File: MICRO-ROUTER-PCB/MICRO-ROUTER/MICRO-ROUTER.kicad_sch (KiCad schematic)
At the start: 41 parts, among them J1 SMA, J2 USB_A, J3 USB_C_Receptacle_USB2.0_16P, J4 Battery Connector, J5 SPI Header, J6 GPIO Header, Q1 FS8205A, SW2 8Devices Reset, SW3 UART Reset, U1 TP4056, U3 CP2102N-Axx-xQFN20, U4 DW01A

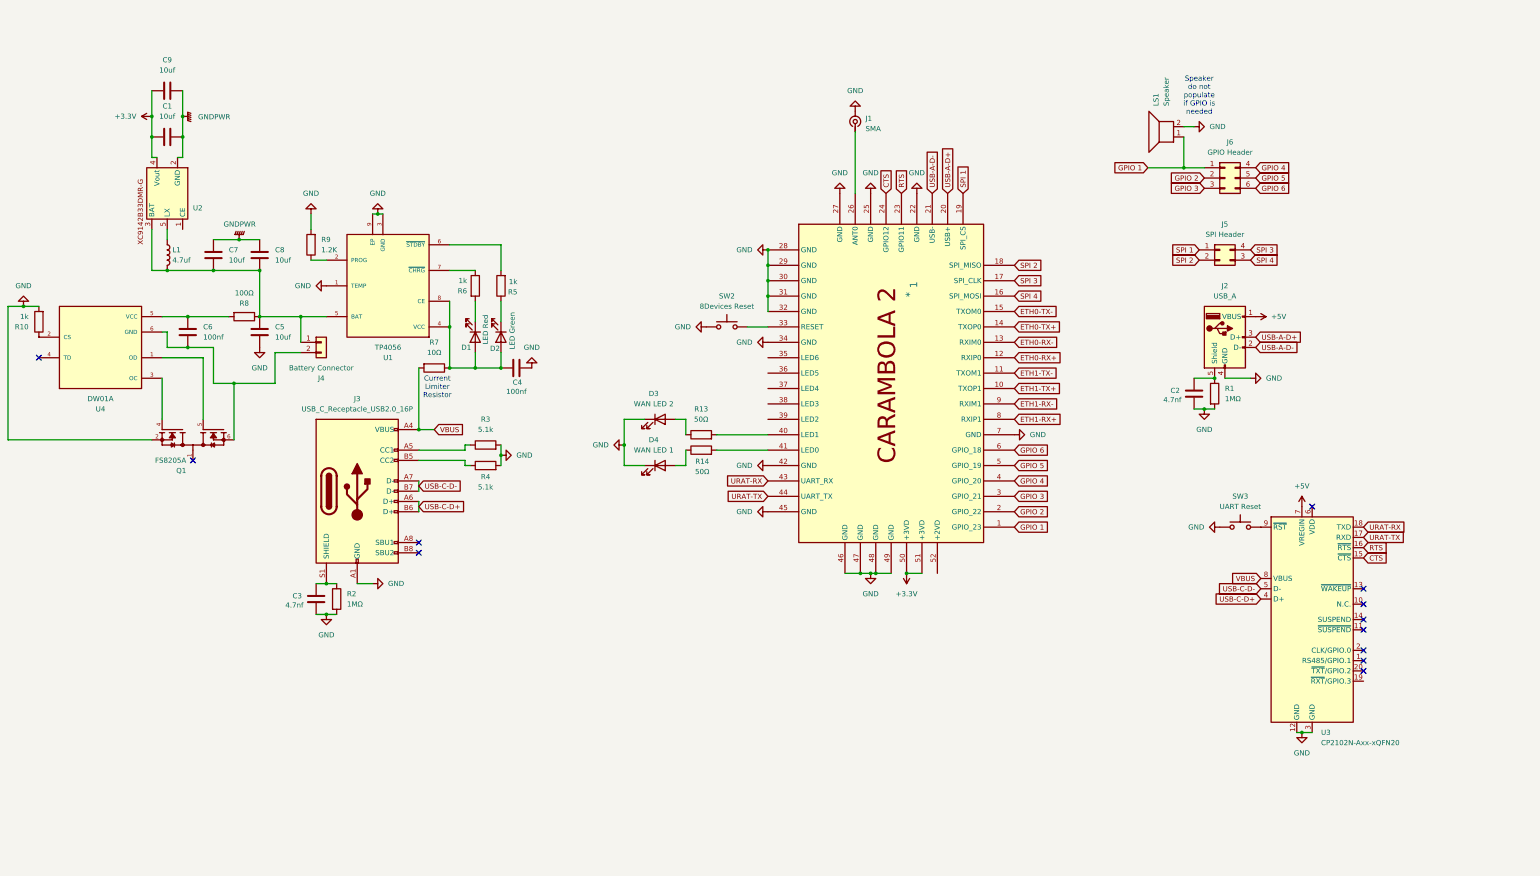
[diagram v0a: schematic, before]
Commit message: Fixed rx tx LEDs Did footprint asociation
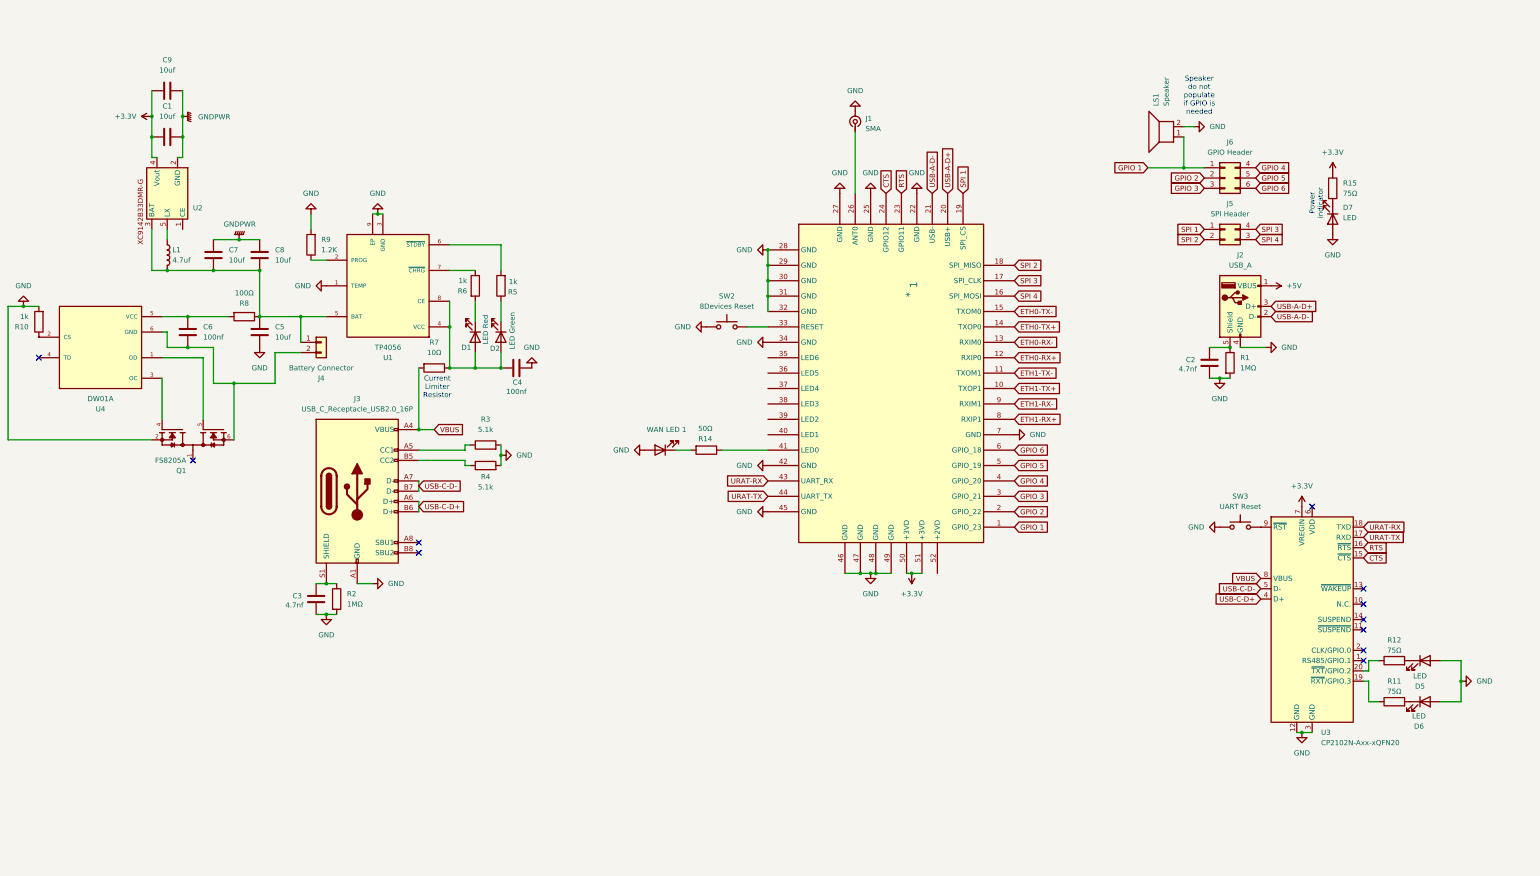
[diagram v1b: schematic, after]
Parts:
- removed D3: WAN LED 2, symbol Device:LED
- removed R13: 50Ω, symbol Device:R
- added D5, D6, D7: LED, LED_SMD:LED_0603_1608Metric, symbol Device:LED
- added R11, R12, R15: 75Ω, Resistor_SMD:R_0603_1608Metric, symbol Device:R
- 1: footprint (none) -> Custom Footprints:8Devices-Carambola2
- C1, C2, C3, C4, C5, C6, C7, C8, C9: footprint (none) -> Capacitor_SMD:C_0603_1608Metric
- D1, D2, D4: footprint (none) -> LED_SMD:LED_0603_1608Metric
- J2: footprint (none) -> Connector_USB:USB_A_Molex_67643_Horizontal
- J3: footprint (none) -> Custom Footprints:TYPE-C-31-M-12
- J4: footprint (none) -> Connector_PinSocket_2.54mm:PinSocket_1x02_P2.54mm_Vertical
- J5: footprint (none) -> Connector_PinSocket_2.54mm:PinSocket_2x02_P2.54mm_Vertical
- J6: footprint (none) -> Connector_PinSocket_2.54mm:PinSocket_2x03_P2.54mm_Vertical
- R1, R10, R14, R2, R3, R4, R5, R6, R7, R8, R9: footprint (none) -> Resistor_SMD:R_0603_1608Metric
- SW2, SW3: footprint (none) -> Button_Switch_THT:SW_PUSH_6mm
- U1, U2: footprint (none) -> Custom Footprints:TP4056
- U4: footprint DW01A:SOT95P280X145-6N -> Custom Footprints:DW01A
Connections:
- net +3.3V: now also U3.7 (VREGIN), R15.1
- net +5V: no longer U3.7 (VREGIN)
- net GND: now also D4.2 (A), D5.2 (A), D6.2 (A), D7.2 (A); no longer D4.1 (K)
- net at R14.1: now also 1.41 (LED0); no longer D4.2 (A)
- net at R14.2: now also D4.1 (K); no longer 1.41 (LED0)
- net at U3.19 (~{RXT}/GPIO.3): now also R11.1
- net at U3.20 (~{TXT}/GPIO.2): now also R12.1
- new net: D6.1 (K), R11.2
- new net: D5.1 (K), R12.2
- new net: D7.1 (K), R15.2
- no-connect marks 12 -> 11
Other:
- note added: "Power indicator"
- moved on the sheet: C2, J2, J5, R1, R14

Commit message: wirred rj45 port and power
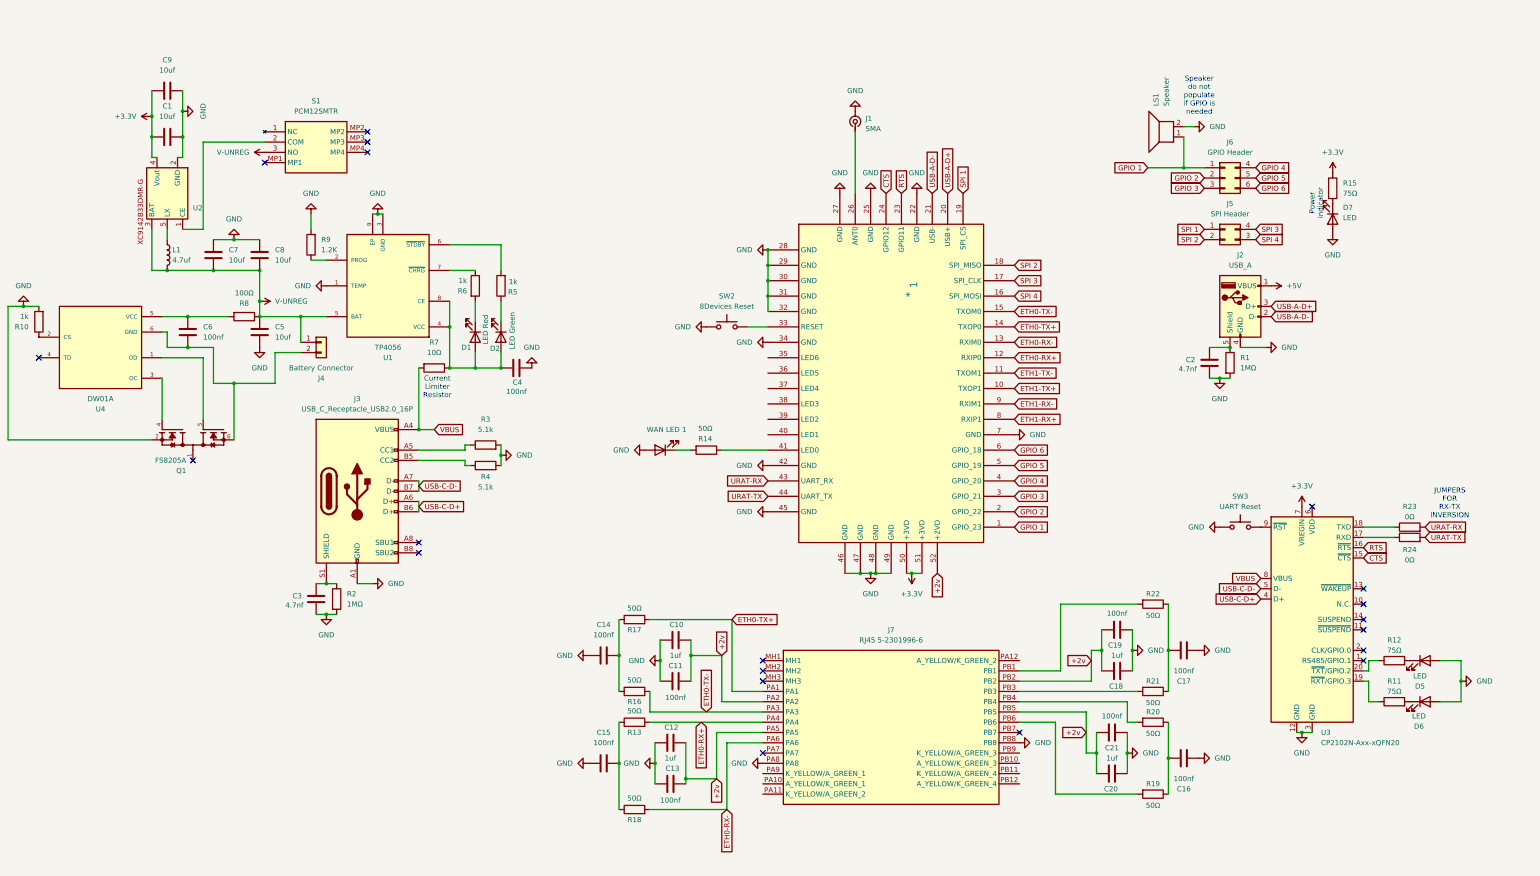
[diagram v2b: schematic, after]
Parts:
- added C10, C12, C18, C20: 1uf, symbol Device:C
- added C11, C13, C14, C15, C16, C17, C19, C21: 100nf, symbol Device:C
- added J7: RJ45 5-2301996-6, 523019966, symbol Custom Symbols:RJ45 5-2301996-6
- added R13, R16, R17, R18, R19, R20, R21, R22: 50Ω, symbol Device:R
- added R23, R24: 0Ω, symbol Device:R
- added S1: PCM12SMTR, PCM12SMTR, symbol Custom Symbols:PCM12SMTR
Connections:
- net GNDPWR is gone; now on net GND: C1.2, C7.2, C8.2, C9.2, U2.2 (GND)
- net ETH0-RX+: now also J7.PA4, R13.2
- net ETH0-RX-: now also J7.PA6, R18.2
- net ETH0-TX+: now also J7.PA1, R17.2
- net ETH0-TX-: now also J7.PA3, R16.2
- net GND: now also C10.1, C11.1, C12.1, C13.1, C14.1, C15.1, C16.1, C17.1, C18.1, C19.1, C20.1, C21.1, J7.PA8, J7.PB8
- net URAT-RX: now also R23.2; no longer U3.18 (TXD)
- net URAT-TX: now also R24.2; no longer U3.17 (RXD)
- net at U2.1 (CE): now also S1.2 (COM)
- net V-UNREG: now reaches C5.2, C7.1, C8.1, J4.1 (Pin_1), L1.2, R8.1, U1.5 (BAT), U2.3 (BAT)
- net V-UNREG: now also S1.3 (NO)
- net +2v: now reaches 1.52 (+2VD)
- net +2v: now also C10.2, C11.2, C12.2, C13.2, C18.2, C19.2, C20.2, C21.2, J7.PA2, J7.PA5, J7.PB2, J7.PB5
- new net: C16.2, R19.1, R20.1
- new net: J7.PB4, R20.2
- new net: R23.1, U3.18 (TXD)
- new net: C14.2, R16.1, R17.1
- new net: R24.1, U3.17 (RXD)
- new net: C17.2, R21.1, R22.1
- new net: J7.PB1, R22.2
- new net: C15.2, R13.1, R18.1
- new net: J7.PB3, R21.2
- new net: J7.PB6, R19.2
- no-connect marks 11 -> 20
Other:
- note added: "JUMPERS FOR RX-TX INVERSION"

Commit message: -Finish rj45 leds -Added notes to schem -Fixed missing footprints -Preped for layout -Wired Eth1
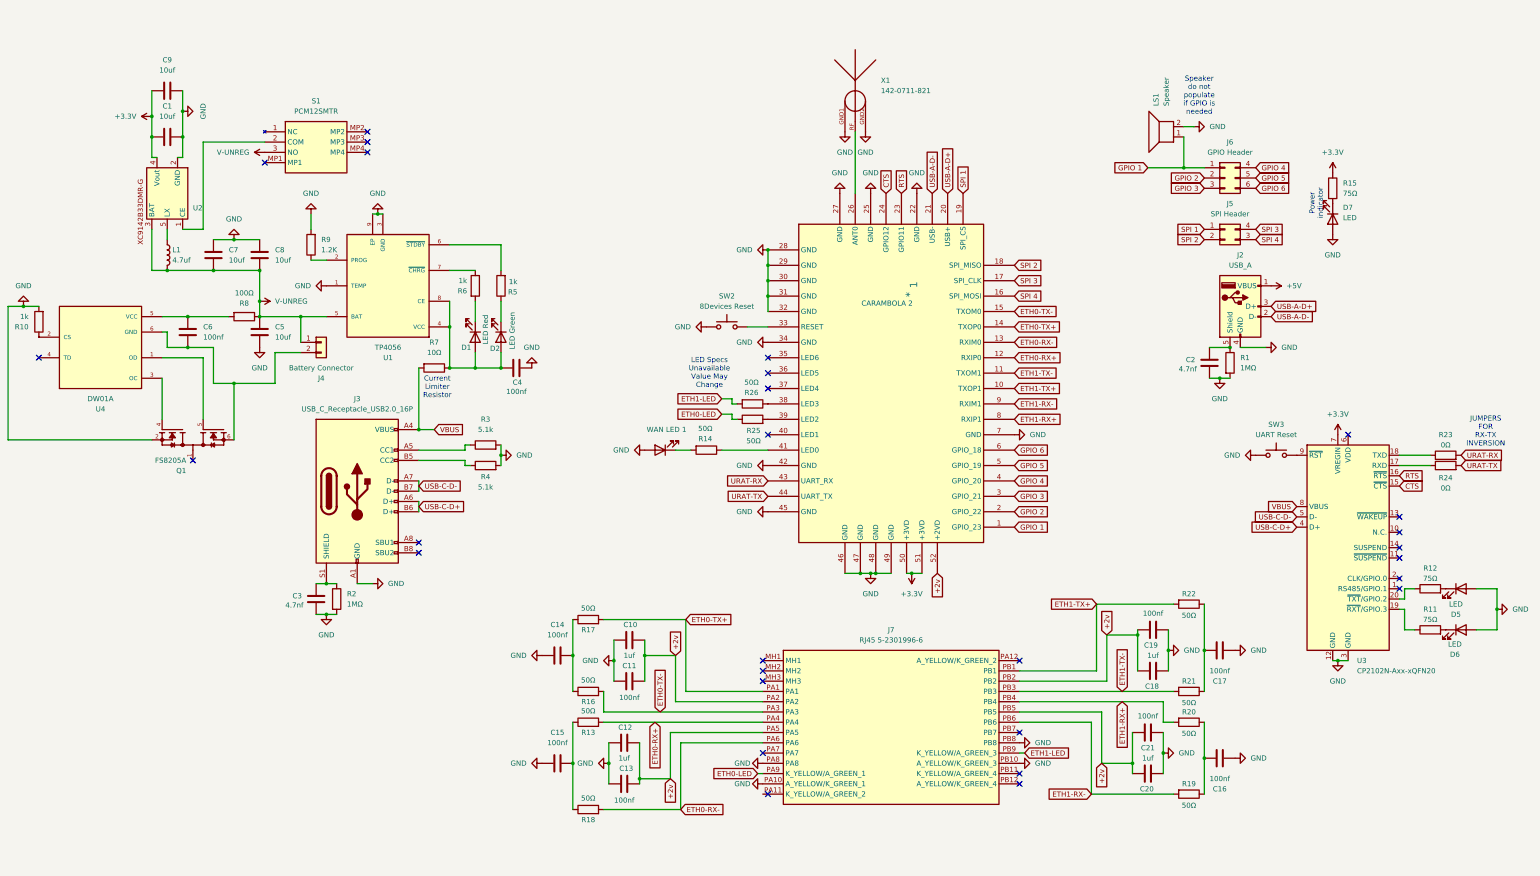
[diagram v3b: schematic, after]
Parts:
- removed J1: SMA, symbol Connector:Conn_Coaxial_Small
- added R25, R26: 50Ω, Resistor_SMD:R_0603_1608Metric, symbol Device:R
- added X1: 142-0711-821, 142-0711-821:142-0711-821, symbol Custom Symbols:142-0711-821
- 1: Name (none) -> CARAMBOLA 2
- C10, C11, C12, C13, C14, C15, C16, C17, C18, C19, C20, C21: footprint (none) -> Capacitor_SMD:C_0603_1608Metric
- J7: footprint 523019966 -> Custom Footprints:RJ45 523019966
- L1: footprint (none) -> Custom Footprints:INDPM5752X300N
- LS1: footprint (none) -> Connector_PinSocket_1.00mm:PinSocket_1x02_P1.00mm_Vertical
- R13, R16, R17, R18, R19, R20, R21, R22, R23, R24: footprint (none) -> Resistor_SMD:R_0603_1608Metric
- S1: footprint PCM12SMTR -> Resistor_SMD:R_0603_1608Metric
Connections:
- net ETH1-RX+: now also J7.PB4, R20.2
- net ETH1-RX-: now also J7.PB6, R19.2
- net ETH1-TX+: now also J7.PB1, R22.2
- net ETH1-TX-: now also J7.PB3, R21.2
- net GND: now also J7.PA10 (A_YELLOW/K_GREEN_1), J7.PB10 (A_YELLOW/K_GREEN_3), X1.GND1, X1.GND2
- net at 1.26 (ANT0): now also X1.RF
- net at 1.38 (LED3): now also R26.1
- net at 1.39 (LED2): now also R25.2
- net ETH0-LED: now reaches J7.PA9 (K_YELLOW/A_GREEN_1)
- net ETH0-LED: now also R25.1
- net ETH1-LED: now reaches J7.PB9 (K_YELLOW/A_GREEN_3)
- net ETH1-LED: now also R26.2
- no-connect marks 20 -> 28
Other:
- note added: "LED Specs Unavailable Value May Change"
- moved on the sheet: C10, C11, C12, C13, C14, C15, C16, C17, C18, C19, C20, C21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

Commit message: fixed footprint error
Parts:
- Q1: footprint FS8205A:SOP65P640X120-8N -> Custom Footprints:FS8205A
- U2: value ~ -> XC9142B33DMR-G; footprint Custom Footprints:TP4056 -> (none)
- U3: footprint Package_DFN_QFN:SiliconLabs_QFN-20-1EP_3x3mm_P0.5mm -> Package_DFN_QFN:SiliconLabs_QFN-20-1EP_3x3mm_P0.5mm_EP1.8x1.8mm
- X1: footprint 142-0711-821:142-0711-821 -> Custom Footprints:SMA 142-0711-821
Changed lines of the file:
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@@
 		(on_board yes)
 		(dnp no)
-		(fields_autoplaced yes)
 		(property "Reference" "U2"
 			(at 69.85 70.9124 90)
@@
 			)
 		)
-		(property "Value" "~"
-			(at 69.85 72.8175 90)
+		(property "Value" " XC9142B33DMR-G "
+			(at 57.15 57.15 0)
 			(effects
 				(font
@@
 			)
 		)
-		(property "Footprint" "Custom Footprints:TP4056"
+		(property "Footprint" ""
 			(at 63.5 67.31 0)
 			(effects
@@
 			)
 		)
-		(property "Footprint" "FS8205A:SOP65P640X120-8N"
+		(property "Footprint" "Custom Footprints:FS8205A"
 			(at 69.85 128.27 0)
 			(effects
@@
 			)
 		)
-		(property "Footprint" "Package_DFN_QFN:SiliconLabs_QFN-20-1EP_3x3mm_P0.5mm"
+		(property "Footprint" "Package_DFN_QFN:SiliconLabs_QFN-20-1EP_3x3mm_P0.5mm_EP1.8x1.8mm"
 			(at 387.35 181.61 0)
 			(effects
@@
 			)
 		)
-		(property "Footprint" "142-0711-821:142-0711-821"
+		(property "Footprint" "Custom Footprints:SMA 142-0711-821"
 			(at 233.68 41.91 0)
 			(effects

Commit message: -began layout -fixed several errors in formating -fixed assocition errors
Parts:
- S1: footprint Resistor_SMD:R_0603_1608Metric -> Custom Footprints:PCM12SMTR
- U2: footprint (none) -> Custom Footprints:XC8107AC20MR-G
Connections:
- net GND: now also Q1.3
- net at Q1.1: now also Q1.8
- net at C6.1, J4.2 (Pin_2), Q1.6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: now also Q1.7
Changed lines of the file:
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@@
 			)
 		)
-		(property "Footprint" ""
+		(property "Footprint" "Custom Footprints:XC8107AC20MR-G"
 			(at 63.5 67.31 0)
 			(effects
@@
 		(pin "4"
 		)
+		(pin "3"
+		)
+		(pin "7"
+		)
+		(pin "8"
+		)
 		(instances
 			(project "MICRO-ROUTER"
@@
 		(fields_autoplaced yes)
 		(property "Reference" "U3"
-			(at 357.7941 182.88 0)
+			(at 357.7941 124.46 0)
 			(effects
 				(font
@@
 		)
 		(property "Value" "CP2102N-Axx-xQFN20"
-			(at 357.7941 185.42 0)
+			(at 357.7941 127 0)
 			(effects
 				(font
@@
 			)
 		)
-		(property "Footprint" "Resistor_SMD:R_0603_1608Metric"
+		(property "Footprint" "Custom Footprints:PCM12SMTR"
 			(at 109.22 146.99 0)
 			(effects

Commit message: -wired sma connector
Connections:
- net ANT1: now reaches 1.26 (ANT0), X1.RF
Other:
- moved on the sheet: X1
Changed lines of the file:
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@@
 	(wire
 		(pts
-			(xy 233.68 52.07) (xy 233.68 67.31)
+			(xy 233.68 41.91) (xy 233.68 67.31)
 		)
 		(stroke
@@
 		)
 	)
+	(hierarchical_label "ANT1"
+		(shape input)
+		(at 233.68 52.07 0)
+		(fields_autoplaced yes)
+		(effects
+			(font
+				(size 1.27 1.27)
+			)
+			(justify left)
+		)
+	)
 	(symbol
 		(lib_id "Connector:USB_C_Receptacle_USB2.0_16P")
@@
 	(symbol
 		(lib_id "power:GND")
-		(at 236.22 52.07 0)
+		(at 236.22 41.91 0)
 		(unit 1)
 		(exclude_from_sim no)
@@
 		(dnp no)
 		(property "Reference" "#PWR050"
-			(at 236.22 58.42 0)
+			(at 236.22 48.26 0)
 			(effects
 				(font
@@
 		)
 		(property "Value" "GND"
-			(at 236.22 57.15 0)
+			(at 236.22 46.99 0)
 			(effects
 				(font
@@
 		)
 		(property "Footprint" ""
-			(at 236.22 52.07 0)
+			(at 236.22 41.91 0)
 			(effects
 				(font
@@
 		)
 		(property "Datasheet" ""
-			(at 236.22 52.07 0)
+			(at 236.22 41.91 0)
 			(effects
 				(font
@@
 		)
 		(property "Description" "Power symbol creates a global label with name \"GND\" , ground"
-			(at 236.22 52.07 0)
+			(at 236.22 41.91 0)
 			(effects
 				(font
@@
 	(symbol
 		(lib_id "power:GND")
-		(at 231.14 52.07 0)
+		(at 231.14 41.91 0)
 		(unit 1)
 		(exclude_from_sim no)
@@
 		(dnp no)
 		(property "Reference" "#PWR03"
-			(at 231.14 58.42 0)
+			(at 231.14 48.26 0)
 			(effects
 				(font
@@
 		)
 		(property "Value" "GND"
-			(at 231.14 57.15 0)
+			(at 231.14 46.99 0)
 			(effects
 				(font
@@
 		)
 		(property "Footprint" ""
-			(at 231.14 52.07 0)
+			(at 231.14 41.91 0)
 			(effects
 				(font
@@
 		)
 		(property "Datasheet" ""
-			(at 231.14 52.07 0)
+			(at 231.14 41.91 0)
 			(effects
 				(font
@@
 		)
 		(property "Description" "Power symbol creates a global label with name \"GND\" , ground"
-			(at 231.14 52.07 0)
+			(at 231.14 41.91 0)
 			(effects
 				(font
@@
 	(symbol
 		(lib_id "Custom Symbols:142-0711-821")
-		(at 233.68 41.91 0)
+		(at 233.68 31.75 0)
 		(unit 1)
 		(exclude_from_sim no)
@@
 		(fields_autoplaced yes)
 		(property "Reference" "X1"
-			(at 240.03 39.3699 0)
+			(at 240.03 29.2099 0)
 			(effects
 				(font
@@
 		)
 		(property "Value" "142-0711-821"
-			(at 240.03 41.9099 0)
+			(at 240.03 31.7499 0)
 			(effects
 				(font
@@
 		)
 		(property "Footprint" "Custom Footprints:SMA 142-0711-821"
-			(at 233.68 41.91 0)
+			(at 233.68 31.75 0)
 			(effects
 				(font
@@
 		)
 		(property "Datasheet" ""
-			(at 233.68 41.91 0)
+			(at 233.68 31.75 0)
 			(effects
 				(font
@@
 		)
 		(property "Description" ""
-			(at 233.68 41.91 0)
+			(at 233.68 31.75 0)
 			(effects
 				(font
@@
 		)
 		(property "MF" "Cinch Connectivity Solutions"
-			(at 233.68 41.91 0)
+			(at 233.68 31.75 0)
 			(effects
 				(font
@@
 		)
 		(property "Description_1" "\nSMA Jack End Launch Round Contact | Johnson-Cinch Connectivity Solutions 142-0711-821\n"
-			(at 233.68 41.91 0)
+			(at 233.68 31.75 0)
 			(effects
 				(font
@@
 		)
 		(property "Package" "None"
-			(at 233.68 41.91 0)
+			(at 233.68 31.75 0)
 			(effects
 				(font
@@
 		)
 		(property "Price" "None"
-			(at 233.68 41.91 0)
+			(at 233.68 31.75 0)
 			(effects
 				(font
@@
 		)
 		(property "SnapEDA_Link" "https://www.snapeda.com/parts/142-0711-821/Cinch+Connectivity+Solutions/view-part/?ref=snap"
-			(at 233.68 41.91 0)
+			(at 233.68 31.75 0)
 			(effects
 				(font
@@
 		)
 		(property "MP" "142-0711-821"
-			(at 233.68 41.91 0)
+			(at 233.68 31.75 0)
 			(effects
 				(font
@@
 		)
 		(property "Availability" "In Stock"
-			(at 233.68 41.91 0)
+			(at 233.68 31.75 0)
 			(effects
 				(font
@@
 		)
 		(property "Check_prices" "https://www.snapeda.com/parts/142-0711-821/Cinch+Connectivity+Solutions/view-part/?ref=eda"
-			(at 233.68 41.91 0)
+			(at 233.68 31.75 0)
 			(effects
 				(font
